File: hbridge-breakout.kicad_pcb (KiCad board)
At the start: 2 copper layers, 28.5 x 38.6 mm, 14 parts, among them J1 Conn_01x10, J2 Conn_01x04, J3 Conn_01x08, U1 74HC00, U2 DRV8870DDA

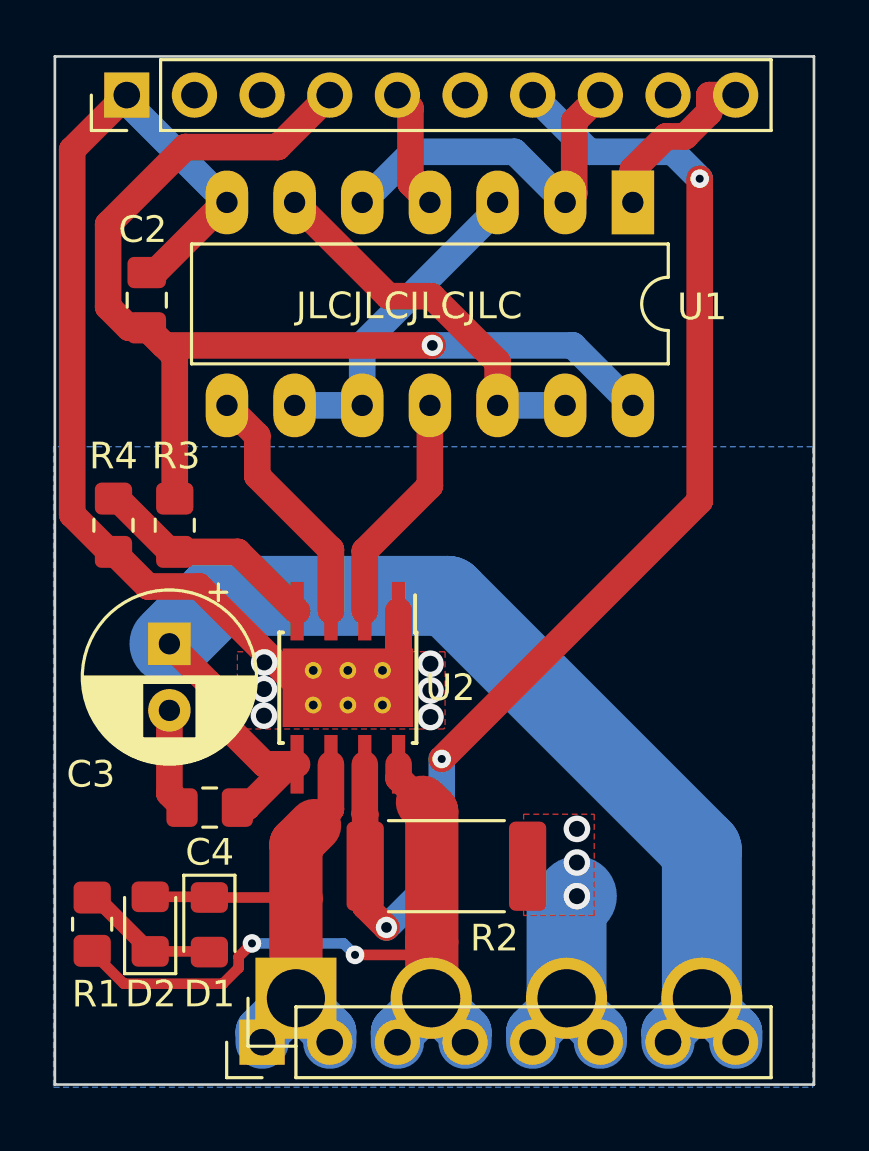
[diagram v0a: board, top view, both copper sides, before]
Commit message: Improved CS trace to not cut the ground plane so much.
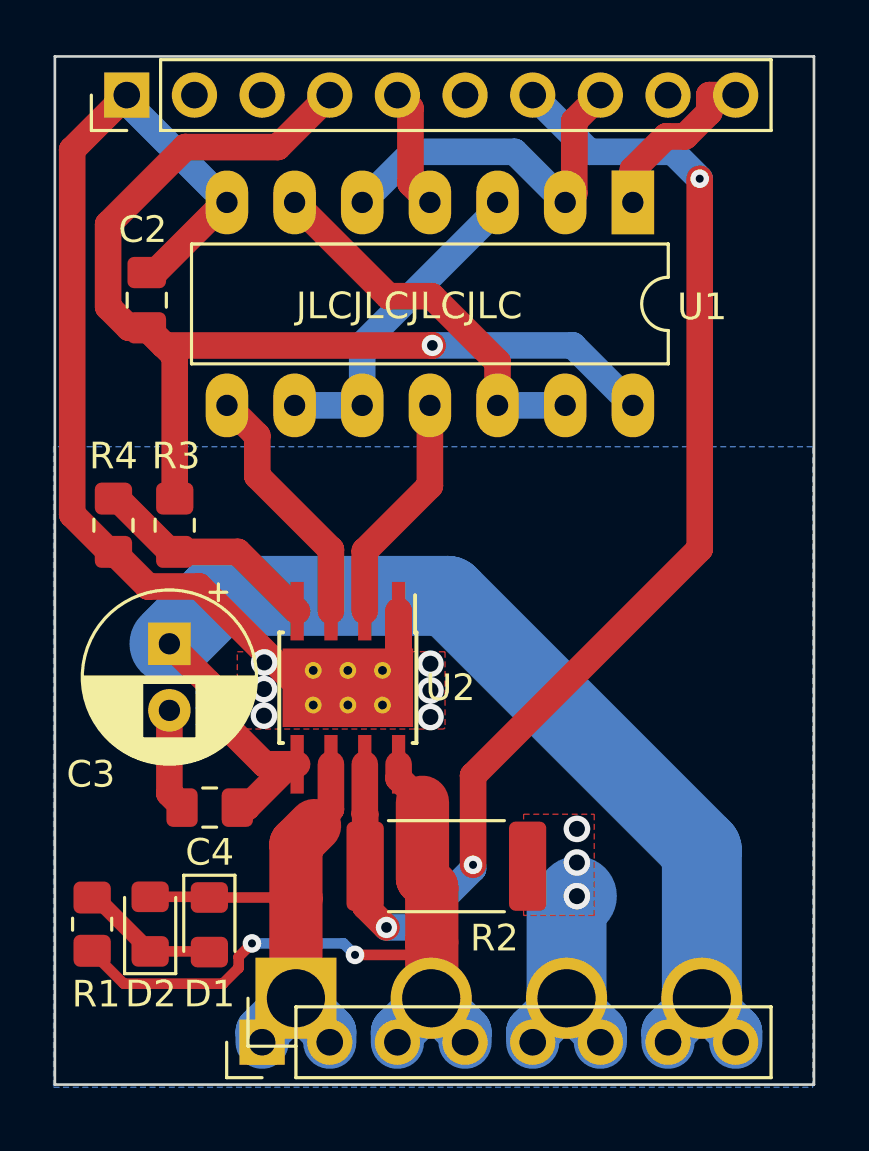
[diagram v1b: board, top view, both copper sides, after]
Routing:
- net /CS: track 47.0 -> 47.6 mm
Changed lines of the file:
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@@
   (segment (start 163.41 77.2) (end 163.9 77.69) (width 1) (layer "F.Cu") (net 7))
   (segment (start 163.9 80.5) (end 164.63 81.23) (width 1) (layer "F.Cu") (net 7))
-  (segment (start 174.76 80.34) (end 174.76 92.44) (width 1) (layer "F.Cu") (net 9))
+  (segment (start 166.25 102.75) (end 166.25 106.100002) (width 1) (layer "F.Cu") (net 9))
   (segment (start 162.2 106.15) (end 162.2 104.2) (width 1) (layer "F.Cu") (net 9))
   (segment (start 162.185 102.325) (end 162.185 104.185) (width 1) (layer "F.Cu") (net 9))
+  (segment (start 174.76 94.24) (end 166.25 102.75) (width 1) (layer "F.Cu") (net 9))
   (segment (start 162.2 104.2) (end 162.185 104.185) (width 1) (layer "F.Cu") (net 9))
   (segment (start 162.2 107.65) (end 163 108.45) (width 1) (layer "F.Cu") (net 9))
-  (segment (start 174.76 92.44) (end 165.075 102.125) (width 1) (layer "F.Cu") (net 9))
+  (segment (start 174.76 80.34) (end 174.76 94.24) (width 1) (layer "F.Cu") (net 9))
   (segment (start 162.2 106.15) (end 162.2 107.65) (width 1) (layer "F.Cu") (net 9))
   (via (at 174.76 80.34) (size 0.7) (drill 0.3) (layers "F.Cu" "B.Cu") (net 9))
   (via (at 163 108.45) (size 0.8) (drill 0.4) (layers "F.Cu" "B.Cu") (net 9))
-  (via (at 165.075 102.125) (size 0.7) (drill 0.3) (layers "F.Cu" "B.Cu") (net 9))
-  (segment (start 165.075 102.125) (end 165.075 106.375) (width 1) (layer "B.Cu") (net 9))
+  (via (at 166.25 106.100002) (size 0.7) (drill 0.3) (layers "F.Cu" "B.Cu") (net 9))
   (segment (start 168.49 77.2) (end 170.62 79.33) (width 1) (layer "B.Cu") (net 9))
+  (segment (start 163 108.45) (end 164.05 108.45) (width 1) (layer "B.Cu") (net 9))
+  (segment (start 166.25 106.25) (end 166.25 106.100002) (width 1) (layer "B.Cu") (net 9))
+  (segment (start 164.05 108.45) (end 166.25 106.25) (width 1) (layer "B.Cu") (net 9))
   (segment (start 173.75 79.33) (end 174.76 80.34) (width 1) (layer "B.Cu") (net 9))
   (segment (start 170.62 79.33) (end 173.75 79.33) (width 1) (layer "B.Cu") (net 9))
-  (segment (start 165.075 106.375) (end 163 108.45) (width 1) (layer "B.Cu") (net 9))
   (segment (start 169.71 81.23) (end 170.05 80.89) (width 1) (layer "F.Cu") (net 10))
   (segment (start 170.05 80.89) (end 170.05 78.18) (width 1) (layer "F.Cu") (net 10))
@@
   (segment (start 157.45 109.969239) (end 157.45 109.55) (width 0.4) (layer "F.Cu") (net 13))
   (segment (start 153.13875 110.56125) (end 156.857989 110.56125) (width 0.4) (layer "F.Cu") (net 13))
+  (segment (start 164.7 109) (end 164.7 106.953459) (width 2) (layer "F.Cu") (net 13))
   (segment (start 164.7 109) (end 164.2195 109.4805) (width 0.4) (layer "F.Cu") (net 13))
   (segment (start 156.857989 110.56125) (end 157.45 109.969239) (width 0.4) (layer "F.Cu") (net 13))
   (segment (start 164.68 111.109) (end 164.7 111.089) (width 2) (layer "F.Cu") (net 13))
   (segment (start 157.45 109.55) (end 157.95 109.05) (width 0.4) (layer "F.Cu") (net 13))
+  (segment (start 164.7 106.953459) (end 164.35 106.603459) (width 2) (layer "F.Cu") (net 13))
   (segment (start 163.455 102.855) (end 164.35 103.75) (width 1) (layer "F.Cu") (net 13))
   (segment (start 164.2195 109.4805) (end 161.8195 109.4805) (width 0.4) (layer "F.Cu") (net 13))
   (segment (start 151.95 109.3725) (end 153.13875 110.56125) (width 0.4) (layer "F.Cu") (net 13))
-  (segment (start 164.7 104.1) (end 164.35 103.75) (width 2) (layer "F.Cu") (net 13))
-  (segment (start 164.7 109) (end 164.7 104.1) (width 2) (layer "F.Cu") (net 13))
+  (segment (start 164.35 106.603459) (end 164.35 103.75) (width 2) (layer "F.Cu") (net 13))
   (segment (start 164.7 111.089) (end 164.7 109) (width 2) (layer "F.Cu") (net 13))
   (via (at 157.95 109.05) (size 0.7) (drill 0.3) (layers "F.Cu" "B.Cu") (net 13))

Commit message: Each direction LED now has its own dropper resistor.
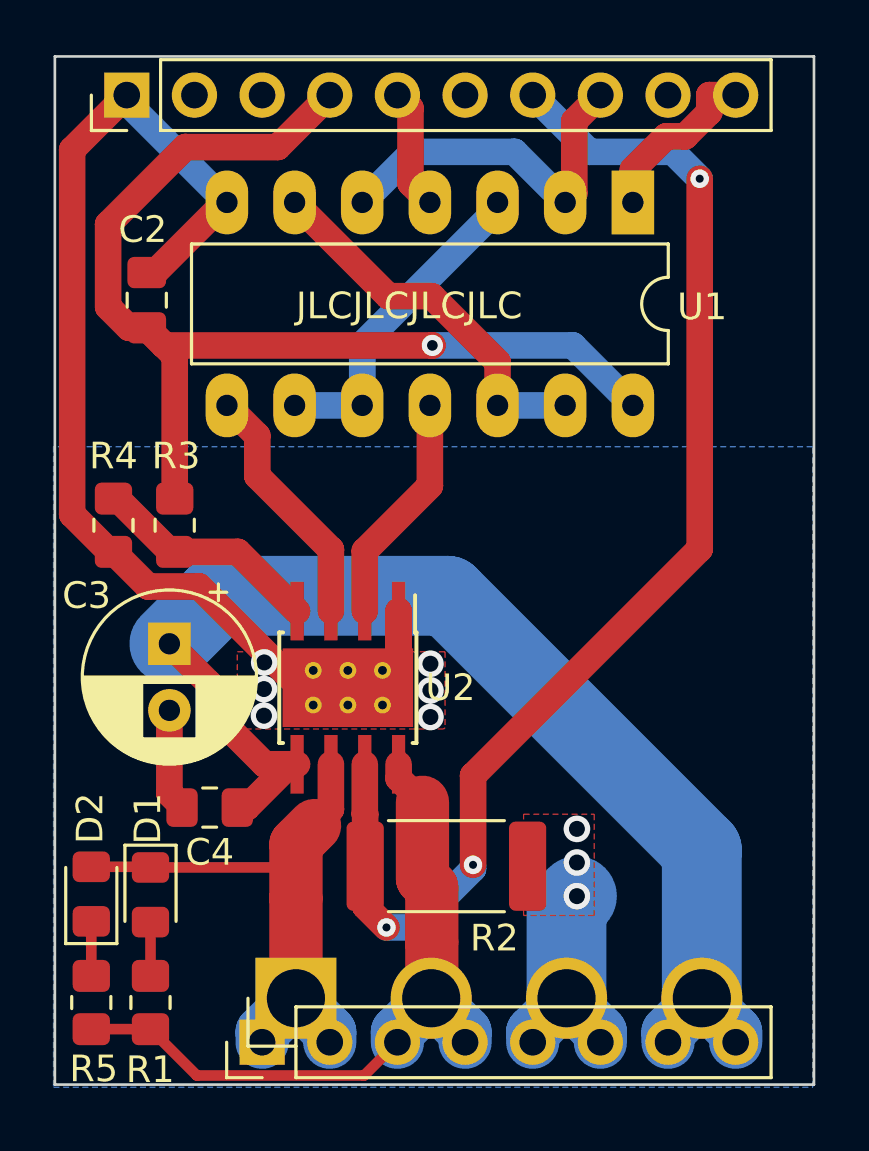
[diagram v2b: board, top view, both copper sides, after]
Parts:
- added R5: 4k7, Resistor_SMD:R_0805_2012Metric_Pad1.20x1.40mm_HandSolder, F.Cu at (151.9, 111.3)
- moved R1 3.67 mm to (154.1, 111.3)
- moved D1 2.48 mm to (154.1, 107.2)
- moved D2 2.48 mm to (151.9, 107.2)
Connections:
- D2 pad 1: Net-(D1-A) -> Net-(D2-K)
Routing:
- net Net-(D1-A): track 5.13 -> 2.02 mm
- net /OUTA: track 19.2 -> 21.8 mm
- net Net-(D2-K): track 0.00 -> 2.05 mm
- net /OUTB: track 28.2 -> 26.4 mm, vias 2 -> 0
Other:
- board text added: "mjd 1.1a 16-Aug-23"
- board text removed: "mjd 1.0a 11-May-23"

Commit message: Added labels to pins
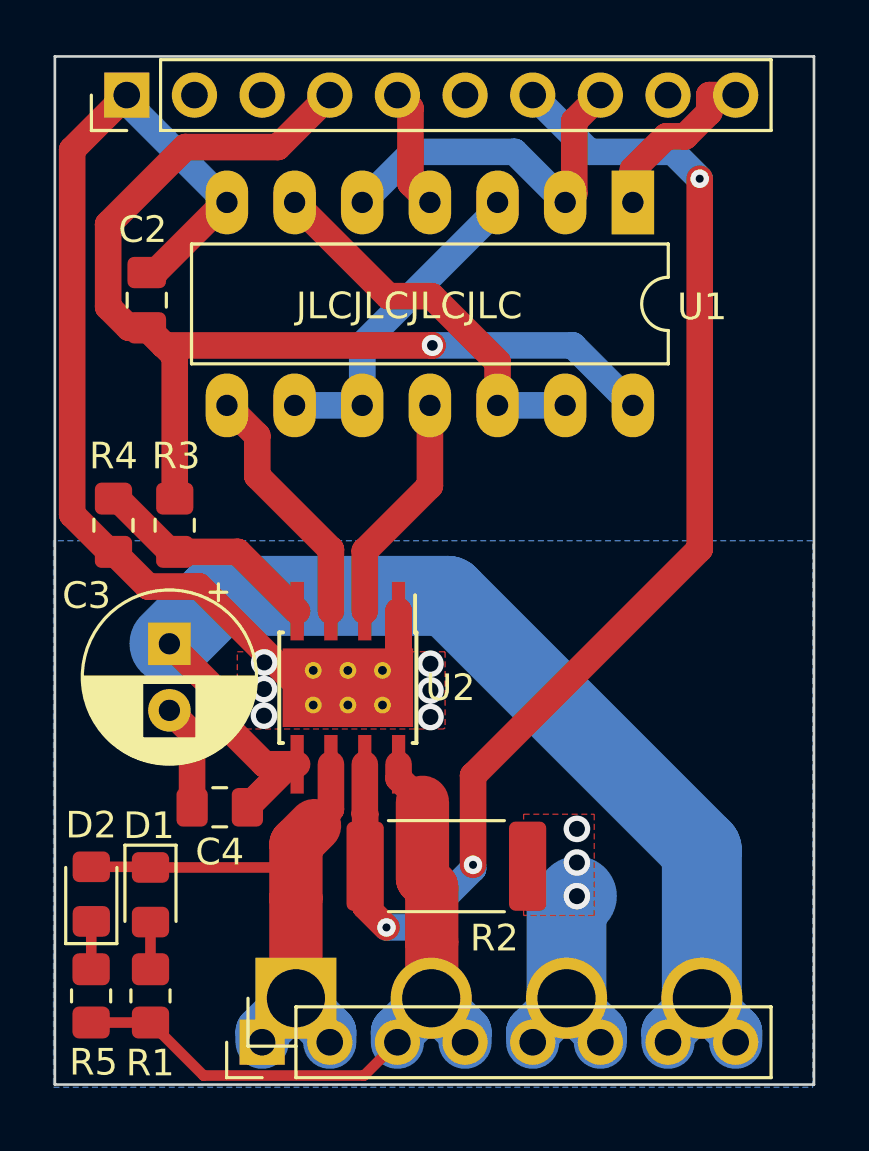
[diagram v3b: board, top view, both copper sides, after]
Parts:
- moved C4 0.38 mm to (156.7, 103.9)
- moved R5 0.25 mm to (151.9, 111.0)
- moved R1 0.25 mm to (154.1, 111.0)
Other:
- board text added: "B+"
- board text added: "B-"
- board text added: "CS"
- board text added: "GND"
- board text added: "INA"
- board text added: "INB"
- board text added: "OUTA"
- board text added: "OUTB"
- board text added: "PWM"
- board text added: "VDD"
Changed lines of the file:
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@@
   )
   (footprint "Capacitor_SMD:C_0805_2012Metric_Pad1.18x1.45mm_HandSolder" (layer "F.Cu")
-    (at 156.3625 103.95 180)
+    (at 156.74 103.94 180)
     (descr "Capacitor SMD 0805 (2012 Metric), square (rectangular) end terminal, IPC_7351 nominal with elongated pad for handsoldering. (Body size source: IPC-SM-782 page 76, https://www.pcb-3d.com/wordpress/wp-content/uploads/ipc-sm-782a_amendment_1_and_2.pdf, https://docs.google.com/spreadsheets/d/1BsfQQcO9C6DZCsRaXUlFlo91Tg2WpOkGARC1WS5S8t0/edit?usp=sharing), generated with kicad-footprint-generator")
     (tags "capacitor handsolder")
@@
     (property "ki_keywords" "LED diode")
     (attr smd)
-    (fp_text reference "D1" (at -2.8525 0.1 90) (layer "F.SilkS")
+    (fp_text reference "D1" (at -2.5925 0.06 -180) (layer "F.SilkS")
         (effects (font (size 1 1) (thickness 0.15)))
     )
@@
     (property "ki_keywords" "LED diode")
     (attr smd)
-    (fp_text reference "D2" (at 2.8475 -0.0475 90) (layer "F.SilkS")
+    (fp_text reference "D2" (at 2.5875 -0.0075 180) (layer "F.SilkS")
         (effects (font (size 1 1) (thickness 0.15)))
     )
@@
   )
   (footprint "Resistor_SMD:R_0805_2012Metric_Pad1.20x1.40mm_HandSolder" (layer "F.Cu")
-    (at 154.14 111.27 -90)
+    (at 154.14 111.02 -90)
     (descr "Resistor SMD 0805 (2012 Metric), square (rectangular) end terminal, IPC_7351 nominal with elongated pad for handsoldering. (Body size source: IPC-SM-782 page 72, https://www.pcb-3d.com/wordpress/wp-content/uploads/ipc-sm-782a_amendment_1_and_2.pdf), generated with kicad-footprint-generator")
     (tags "resistor handsolder")
@@
   )
   (footprint "Resistor_SMD:R_0805_2012Metric_Pad1.20x1.40mm_HandSolder" (layer "F.Cu")
-    (at 151.9175 111.27 -90)
+    (at 151.91 111.02 -90)
     (descr "Resistor SMD 0805 (2012 Metric), square (rectangular) end terminal, IPC_7351 nominal with elongated pad for handsoldering. (Body size source: IPC-SM-782 page 72, https://www.pcb-3d.com/wordpress/wp-content/uploads/ipc-sm-782a_amendment_1_and_2.pdf), generated with kicad-footprint-generator")
     (tags "resistor handsolder")
@@
   (gr_rect (start 150.55 75.75) (end 179.05 114.35)
     (stroke (width 0.1) (type default)) (fill none) (layer "Edge.Cuts"))
-  (gr_text "mjd 1.1a 16-Aug-23" (at 177.2 86.9) (layer "B.SilkS")
+  (gr_text "GND" (at 153.8 78.03 90) (layer "B.SilkS")
+    (effects (font (size 0.8 0.8) (thickness 0.16) bold) (justify left bottom mirror))
+  )
+  (gr_text "PWM" (at 171.58 78.03 90) (layer "B.SilkS")
+    (effects (font (size 0.8 0.8) (thickness 0.16) bold) (justify left bottom mirror))
+  )
+  (gr_text "B+" (at 175.6 109.37 90) (layer "B.SilkS")
+    (effects (font (size 1.2 1.2) (thickness 0.24) bold) (justify right bottom mirror))
+  )
+  (gr_text "B-" (at 170.52 109.37 90) (layer "B.SilkS")
+    (effects (font (size 1.2 1.2) (thickness 0.24) bold) (justify right bottom mirror))
+  )
+  (gr_text "VDD" (at 161.42 78.03 90) (layer "B.SilkS")
+    (effects (font (size 0.8 0.8) (thickness 0.16) bold) (justify left bottom mirror))
+  )
+  (gr_text "INB" (at 163.96 78.03 90) (layer "B.SilkS")
+    (effects (font (size 0.8 0.8) (thickness 0.16) bold) (justify left bottom mirror))
+  )
+  (gr_text "OUTA" (at 160.36 109.37 90) (layer "B.SilkS")
+    (effects (font (size 1.2 1.2) (thickness 0.24) bold) (justify right bottom mirror))
+  )
+  (gr_text "mjd 1.1a 16-Aug-23" (at 177.95 81.25 90) (layer "B.SilkS")
     (effects (font (size 1.5 1.5) (thickness 0.3) bold) (justify left bottom mirror))
   )
-  (gr_text "h-bridge breakout" (at 176.2 84.55) (layer "B.SilkS")
+  (gr_text "h-bridge breakout" (at 175.6 82.25 90) (layer "B.SilkS")
     (effects (font (size 1.5 1.5) (thickness 0.3) bold) (justify left bottom mirror))
+  )
+  (gr_text "INA" (at 176.66 78.03 90) (layer "B.SilkS")
+    (effects (font (size 0.8 0.8) (thickness 0.16) bold) (justify left bottom mirror))
+  )
+  (gr_text "CS" (at 169.04 78.03 90) (layer "B.SilkS")
+    (effects (font (size 0.8 0.8) (thickness 0.16) bold) (justify left bottom mirror))
+  )
+  (gr_text "OUTB" (at 165.44 109.37 90) (layer "B.SilkS")
+    (effects (font (size 1.2 1.2) (thickness 0.24) bold) (justify right bottom mirror))
   )
   (gr_text "JLCJLCJLCJLC" (at 159.6 85.7) (layer "F.SilkS")
@@
   (segment (start 162.78 99.45) (end 161.65 99.45) (width 1) (layer "F.Cu") (net 2))
   (segment (start 154.05 95.65) (end 155.97 95.65) (width 1) (layer "F.Cu") (net 2))
-  (segment (start 155.325 103.95) (end 155.325 103.893503) (width 1) (layer "F.Cu") (net 2))
-  (segment (start 154.85 103.418503) (end 154.85 100.3) (width 1) (layer "F.Cu") (net 2))
   (segment (start 161.55 99.45) (end 162.325 98.675) (width 1) (layer "F.Cu") (net 2))
   (segment (start 162.68 99.45) (end 161.55 99.45) (width 1) (layer "F.Cu") (net 2))
@@
   (segment (start 151.2 79.25) (end 153.25 77.2) (width 1) (layer "F.Cu") (net 2))
   (segment (start 152.606497 94.35) (end 151.2 92.943503) (width 1) (layer "F.Cu") (net 2))
+  (segment (start 155.7025 103.94) (end 155.7025 101.152494) (width 1) (layer "F.Cu") (net 2))
+  (segment (start 155.7025 101.152494) (end 154.849994 100.299988) (width 1) (layer "F.Cu") (net 2))
   (segment (start 152.75 94.35) (end 152.606497 94.35) (width 1) (layer "F.Cu") (net 2))
   (segment (start 162.325 98.675) (end 163.455 98.675) (width 1) (layer "F.Cu") (net 2))
@@
   (segment (start 154.3 83.8625) (end 154 83.8625) (width 1) (layer "F.Cu") (net 2))
   (segment (start 163.455 96.575) (end 163.455 98.675) (width 1) (layer "F.Cu") (net 2))
-  (segment (start 155.325 103.893503) (end 154.85 103.418503) (width 1) (layer "F.Cu") (net 2))
   (via (at 158.4 99.5) (size 1) (drill 0.6) (layers "F.Cu" "B.Cu") (free) (net 2))
   (via (at 170.15 106.0125) (size 1) (drill 0.6) (layers "F.Cu" "B.Cu") (free) (net 2))
@@
   (segment (start 168.49 112.379) (end 169.76 111.109) (width 2) (layer "B.Cu") (net 2))
   (segment (start 169.76 111.109) (end 169.76 107.665) (width 3) (layer "B.Cu") (net 2))
-  (segment (start 157.75 103.95) (end 159.375 102.325) (width 1) (layer "F.Cu") (net 3))
-  (segment (start 154.85 97.8) (end 156.35 99.3) (width 1) (layer "F.Cu") (net 3))
-  (segment (start 157.4 103.95) (end 157.75 103.95) (width 1) (layer "F.Cu") (net 3))
-  (segment (start 156.35 99.3) (end 156.35 100.25) (width 1) (layer "F.Cu") (net 3))
+  (segment (start 157.7775 103.9225) (end 159.375 102.325) (width 1) (layer "F.Cu") (net 3))
   (segment (start 158.425 102.325) (end 159.375 102.325) (width 1) (layer "F.Cu") (net 3))
-  (segment (start 156.35 100.25) (end 158.425 102.325) (width 1) (layer "F.Cu") (net 3))
+  (segment (start 156.9025 100.8025) (end 158.425 102.325) (width 1) (layer "F.Cu") (net 3))
+  (segment (start 157.7775 103.94) (end 157.7775 103.9225) (width 1) (layer "F.Cu") (net 3))
+  (segment (start 156.9025 99.8525) (end 156.9025 100.8025) (width 1) (layer "F.Cu") (net 3))
   (segment (start 159.375 102.325) (end 159.645 102.325) (width 1) (layer "F.Cu") (net 3))
+  (segment (start 154.85 97.8) (end 156.9025 99.8525) (width 1) (layer "F.Cu") (net 3))
   (segment (start 174.84 111.109) (end 174.84 105.54) (width 3) (layer "B.Cu") (net 3))
   (segment (start 173.57 112.379) (end 174.84 111.109) (width 2) (layer "B.Cu") (net 3))
@@
   (segment (start 164.7 106.953459) (end 164.35 106.603459) (width 2) (layer "F.Cu") (net 13))
   (segment (start 163.455 102.855) (end 164.35 103.75) (width 1) (layer "F.Cu") (net 13))
+  (segment (start 154.14 112.02) (end 156.13 114.01) (width 0.4) (layer "F.Cu") (net 13))
   (segment (start 162.16 114.01) (end 163.41 112.76) (width 0.4) (layer "F.Cu") (net 13))
-  (segment (start 154.14 112.27) (end 155.88 114.01) (width 0.4) (layer "F.Cu") (net 13))
-  (segment (start 151.9175 112.27) (end 154.14 112.27) (width 0.4) (layer "F.Cu") (net 13))
+  (segment (start 156.13 114.01) (end 162.16 114.01) (width 0.4) (layer "F.Cu") (net 13))
   (segment (start 164.35 106.603459) (end 164.35 103.75) (width 2) (layer "F.Cu") (net 13))
+  (segment (start 151.91 112.02) (end 154.14 112.02) (width 0.4) (layer "F.Cu") (net 13))
   (segment (start 164.7 111.089) (end 164.7 109) (width 2) (layer "F.Cu") (net 13))
-  (segment (start 155.88 114.01) (end 162.16 114.01) (width 0.4) (layer "F.Cu") (net 13))
   (segment (start 165.95 112.76) (end 165.95 112.379) (width 2) (layer "B.Cu") (net 13))
   (segment (start 165.95 112.379) (end 164.68 111.109) (width 2) (layer "B.Cu") (net 13))
@@
   (segment (start 167.17 81.48) (end 162.09 86.56) (width 1) (layer "B.Cu") (net 18))
   (segment (start 167.17 81.23) (end 167.17 81.48) (width 1) (layer "B.Cu") (net 18))
-  (segment (start 154.14 108.2475) (end 154.14 110.27) (width 0.4) (layer "F.Cu") (net 19))
-  (segment (start 151.9175 108.2225) (end 151.9175 110.27) (width 0.4) (layer "F.Cu") (net 20))
+  (segment (start 154.14 108.2475) (end 154.14 110.02) (width 0.4) (layer "F.Cu") (net 19))
+  (segment (start 151.9175 108.2225) (end 151.9175 110.0125) (width 0.4) (layer "F.Cu") (net 20))
+  (segment (start 151.9175 110.0125) (end 151.91 110.02) (width 0.4) (layer "F.Cu") (net 20))
   (zone (net 2) (net_name "GND") (layer "F.Cu") (hatch edge 0.5)
     (priority 2)
@@
         (xy 150.5 114.45)
         (xy 179 114.45)
-        (xy 179 90.4)
-        (xy 150.5 90.4)
+        (xy 179 93.93)
+        (xy 150.5 93.93)
       )
     )
